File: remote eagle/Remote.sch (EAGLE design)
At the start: 25 parts, among them IC1 TINY24/44/84-MU, J1 ISP Touch, U1 NRF24L01ALT1, Y1 8MHz, Y2 ANTENNA2SMD5

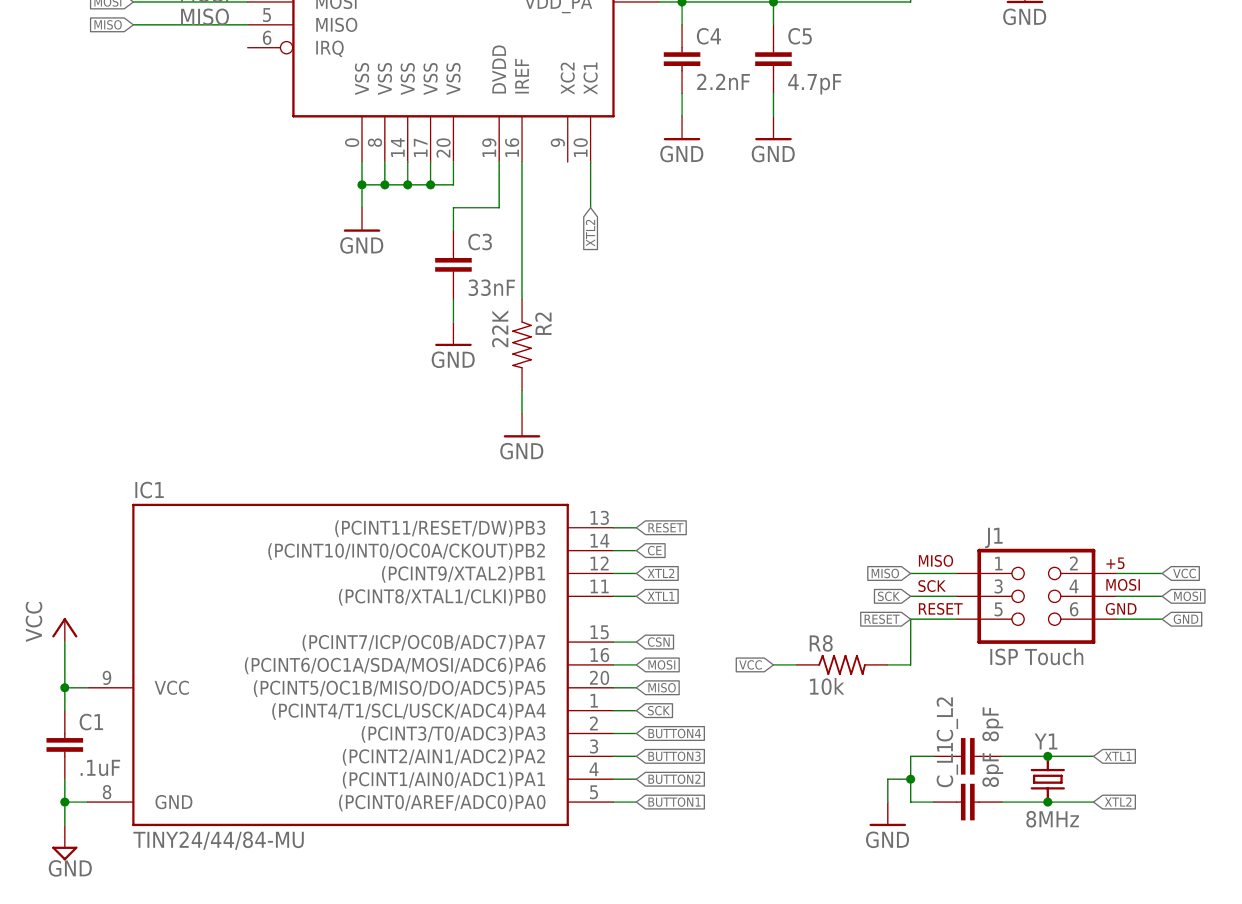
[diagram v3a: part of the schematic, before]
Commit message: Moving from MFL package to QFN package for ATTiny84A MCU.
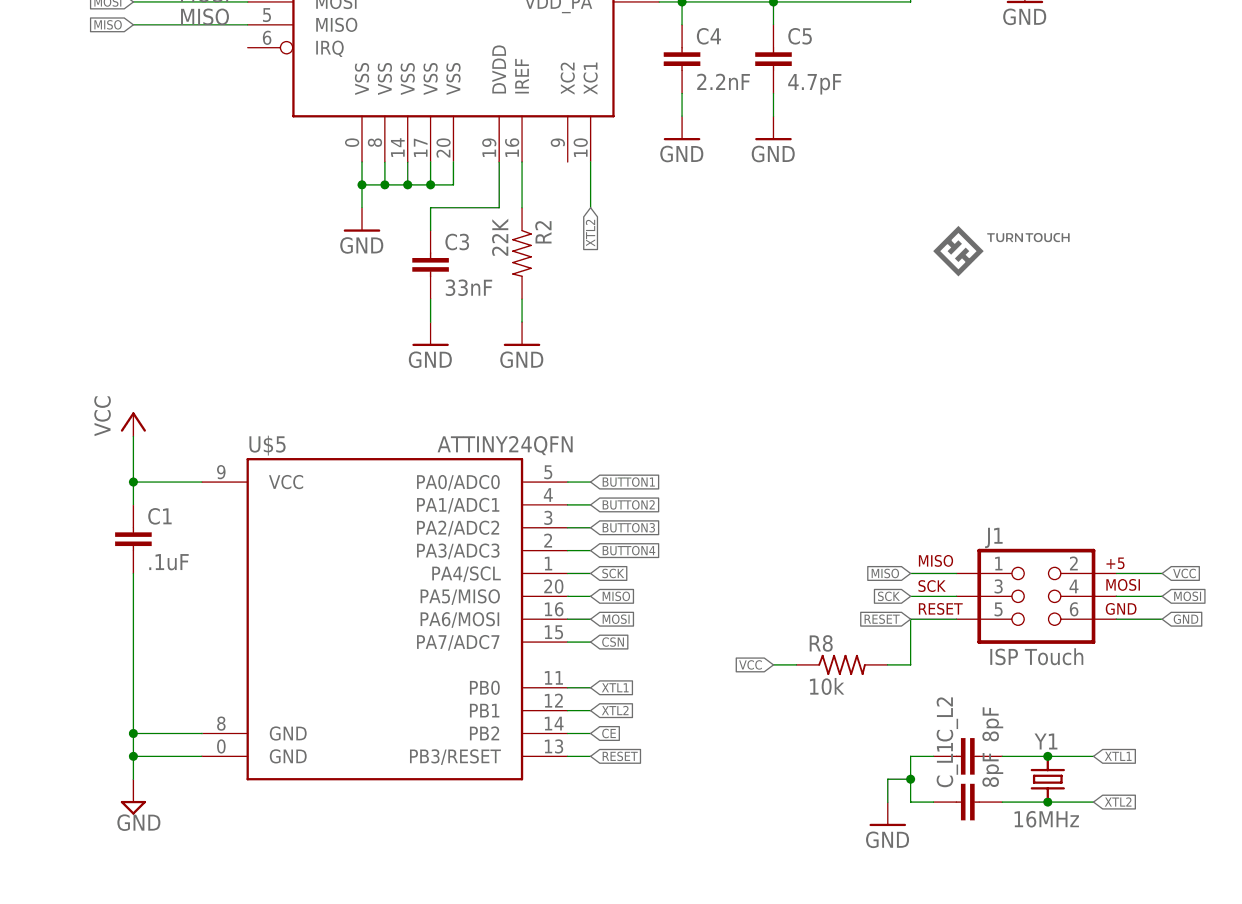
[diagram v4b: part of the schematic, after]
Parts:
- removed IC1: TINY24/44/84-MU, avr-7:TINY24/44/84-MU
- added U$5: ATTINY24QFN, SparkFun-DigitalIC:ATTINY24QFN
- Y1: value 8MHz -> 16MHz; device remote:CRYSTAL8X4.5 -> remote:CRYSTAL5X3.2
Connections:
- net BUTTON1: now also U$5.PA0/ADC0; no longer IC1.(PCINT0/AREF/ADC0)PA0
- net BUTTON2: now also U$5.PA1/ADC1; no longer IC1.(PCINT1/AIN0/ADC1)PA1
- net BUTTON3: now also U$5.PA2/ADC2; no longer IC1.(PCINT2/AIN1/ADC2)PA2
- net BUTTON4: now also U$5.PA3/ADC3; no longer IC1.(PCINT3/T0/ADC3)PA3
- net CE: now also U$5.PB2; no longer IC1.(PCINT10/INT0/OC0A/CKOUT)PB2
- net CSN: now also U$5.PA7/ADC7; no longer IC1.(PCINT7/ICP/OC0B/ADC7)PA7
- net GND: now also U$5.GND, U$5.GND@0; no longer IC1.GND
- net MISO: now also U$5.PA5/MISO; no longer IC1.(PCINT5/OC1B/MISO/DO/ADC5)PA5
- net MOSI: now also U$5.PA6/MOSI; no longer IC1.(PCINT6/OC1A/SDA/MOSI/ADC6)PA6
- net RESET: now also U$5.PB3/RESET; no longer IC1.(PCINT11/RESET/DW)PB3
- net SCK: now also U$5.PA4/SCL; no longer IC1.(PCINT4/T1/SCL/USCK/ADC4)PA4
- net VCC: now also U$5.VCC; no longer IC1.VCC
- net XTL1: now also U$5.PB0; no longer IC1.(PCINT8/XTAL1/CLKI)PB0
- net XTL2: now also U$5.PB1; no longer IC1.(PCINT9/XTAL2)PB1
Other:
- moved on the sheet: C1, C3, R2

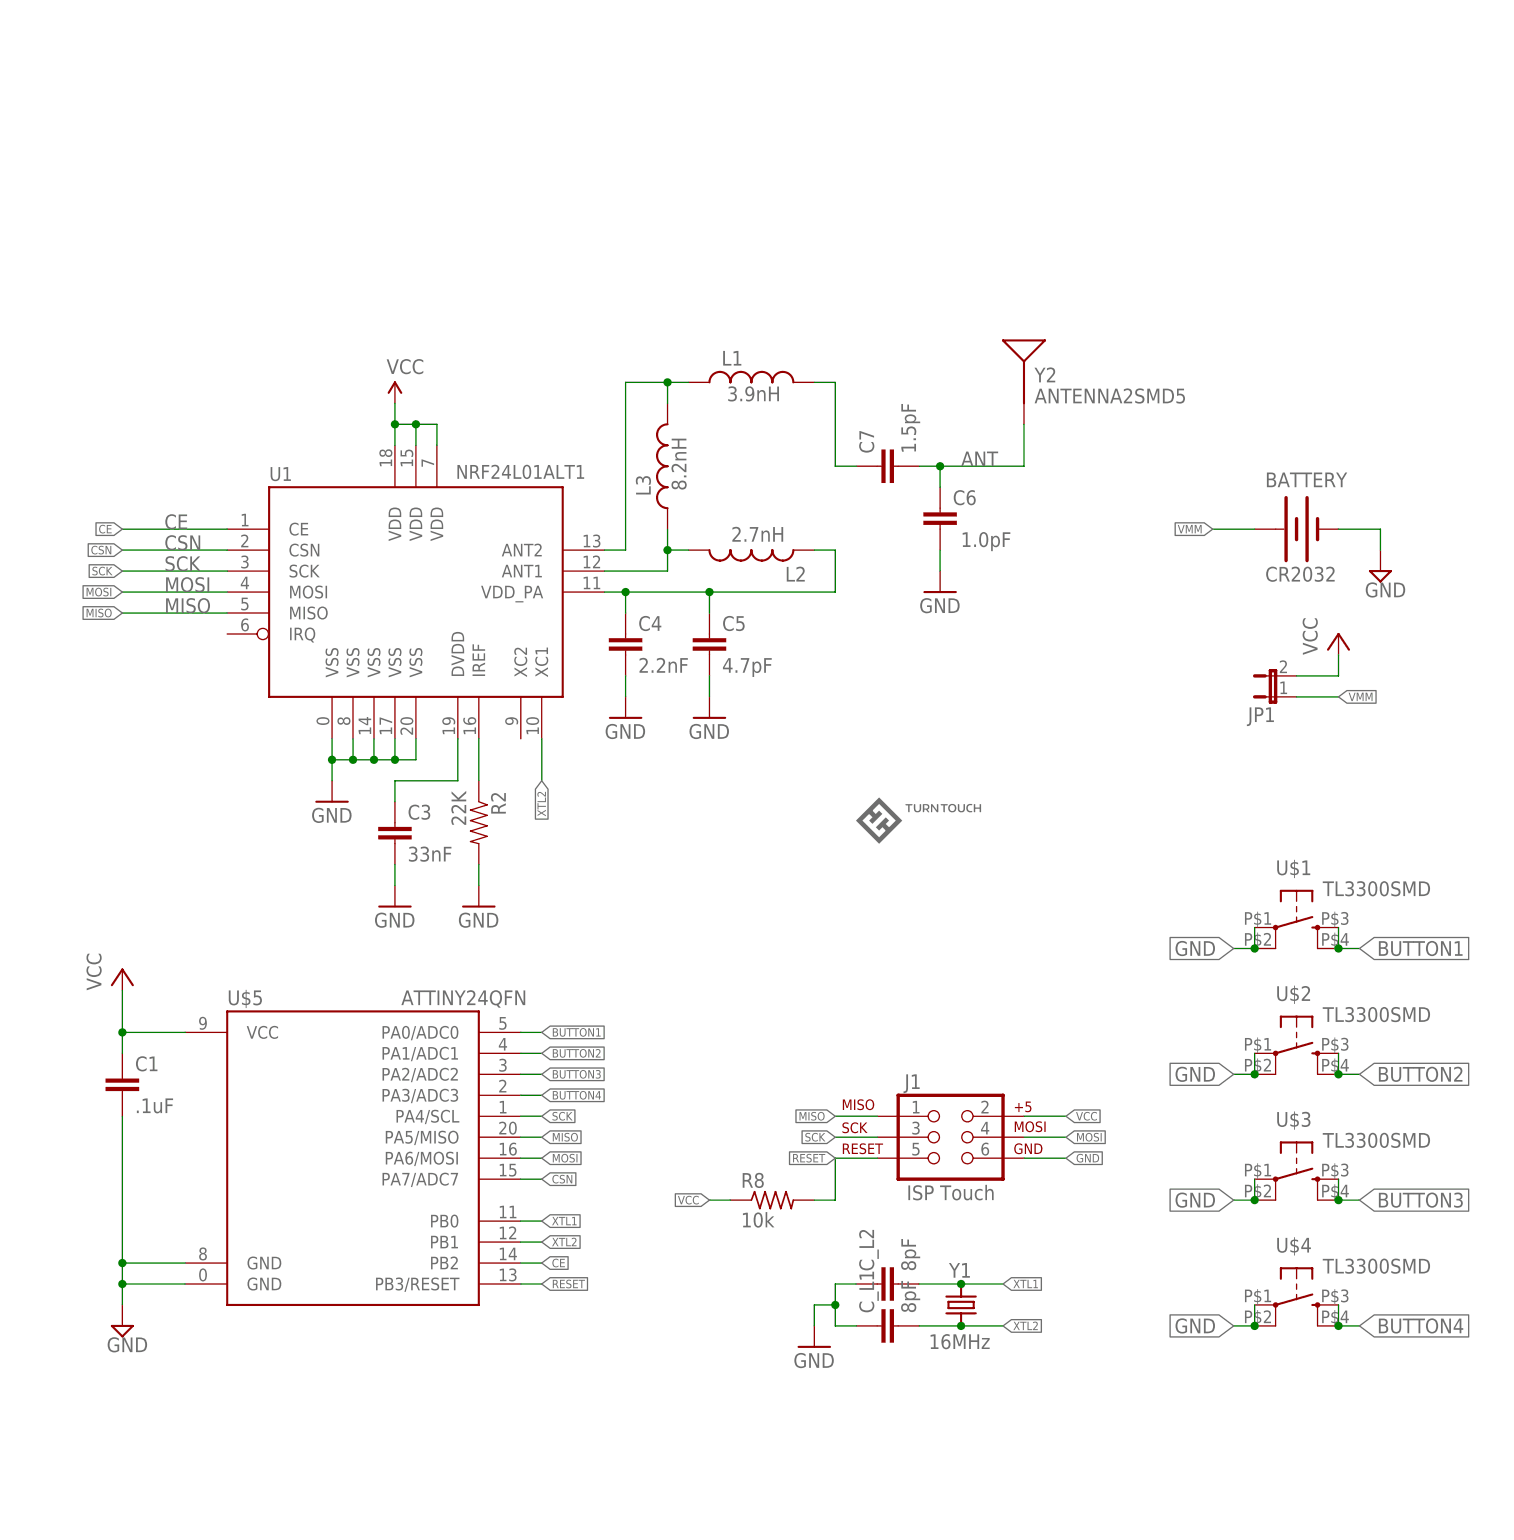
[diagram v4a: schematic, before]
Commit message: Moving code into src/ and libs/.
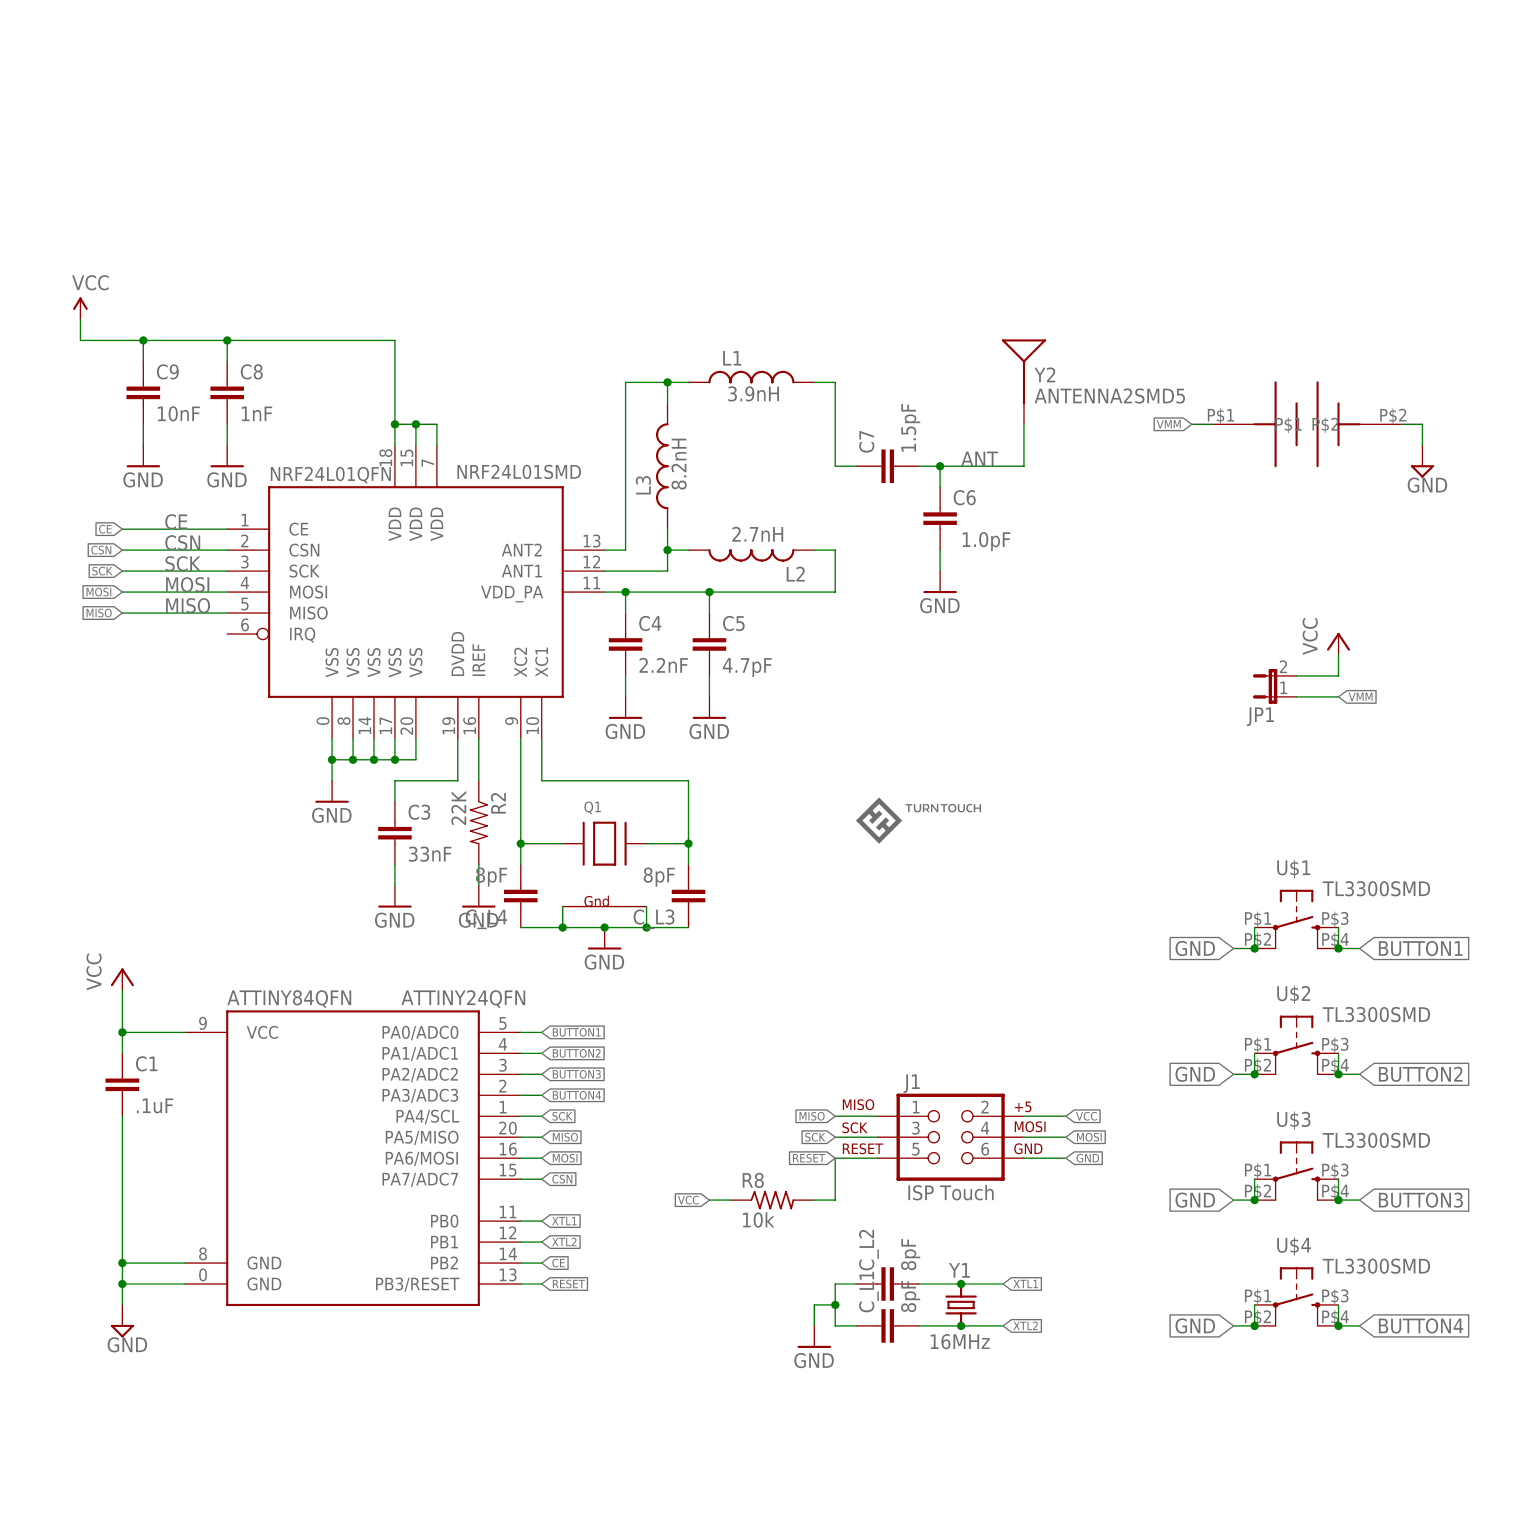
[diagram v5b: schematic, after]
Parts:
- removed BATTERY: CR2032, SparkFun-Electromechanical:BATTERY20MM_4LEGS_OVERPASTE
- removed U1: NRF24L01ALT1, Testing:NRF24L01ALT1
- added C8: 1nF, SparkFun:CAP0402-CAP
- added C9: 10nF, SparkFun:CAP0402-CAP
- added C_L3, C_L4: 8pF, SparkFun-Passives:CAP0402-CAP
- added NRF24L01QFN: NRF24L01SMD, Testing:NRF24L01SMD
- added Q1: (no value), adafruit:XTAL-4-3225
- added U$6: COINCELLHOLDER, remote:COINCELLHOLDER
- renumbered U$5 to ATTINY84QFN
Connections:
- new net N$2: C_L4.2, NRF24L01QFN.XC2, Q1.X1
- new net N$3: C_L3.2, NRF24L01QFN.XC1, Q1.X2
- net CE: now also NRF24L01QFN.CE; no longer U1.CE
- net CSN: now also NRF24L01QFN.CSN; no longer U1.CSN
- net GND: now also C8.2, C9.2, C_L3.1, C_L4.1, NRF24L01QFN.VSS@0, NRF24L01QFN.VSS@14, NRF24L01QFN.VSS@17, NRF24L01QFN.VSS@20, NRF24L01QFN.VSS@8, Q1.G1, Q1.G2, U$6.P$2; no longer BATTERY.-, U1.VSS@0, U1.VSS@14, U1.VSS@17, U1.VSS@20, U1.VSS@8
- net MISO: now also NRF24L01QFN.MISO; no longer U1.MISO
- net MOSI: now also NRF24L01QFN.MOSI; no longer U1.MOSI
- net N$4: now also NRF24L01QFN.IREF; no longer U1.IREF
- net N$5: now also NRF24L01QFN.DVDD; no longer U1.DVDD
- net N$6: now also NRF24L01QFN.ANT2; no longer U1.ANT2
- net N$7: now also NRF24L01QFN.VDD_PA; no longer U1.VDD_PA
- net N$8: now also NRF24L01QFN.ANT1; no longer U1.ANT1
- net SCK: now also NRF24L01QFN.SCK; no longer U1.SCK
- net VCC: now also C8.1, C9.1, NRF24L01QFN.VDD@15, NRF24L01QFN.VDD@18, NRF24L01QFN.VDD@7; no longer U1.VDD@15, U1.VDD@18, U1.VDD@7
- net VMM: now also U$6.P$1; no longer BATTERY.+
- net XTL2: no longer U1.XC1
